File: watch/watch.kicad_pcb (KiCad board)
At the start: 2 copper layers, 36 x 36 mm, 102 parts, among them IC1 IS32FL3237-TQLA3-TR, SW1 ButtonWakeup, U1 STM32L031F4Px, Y1 CR_32kHz

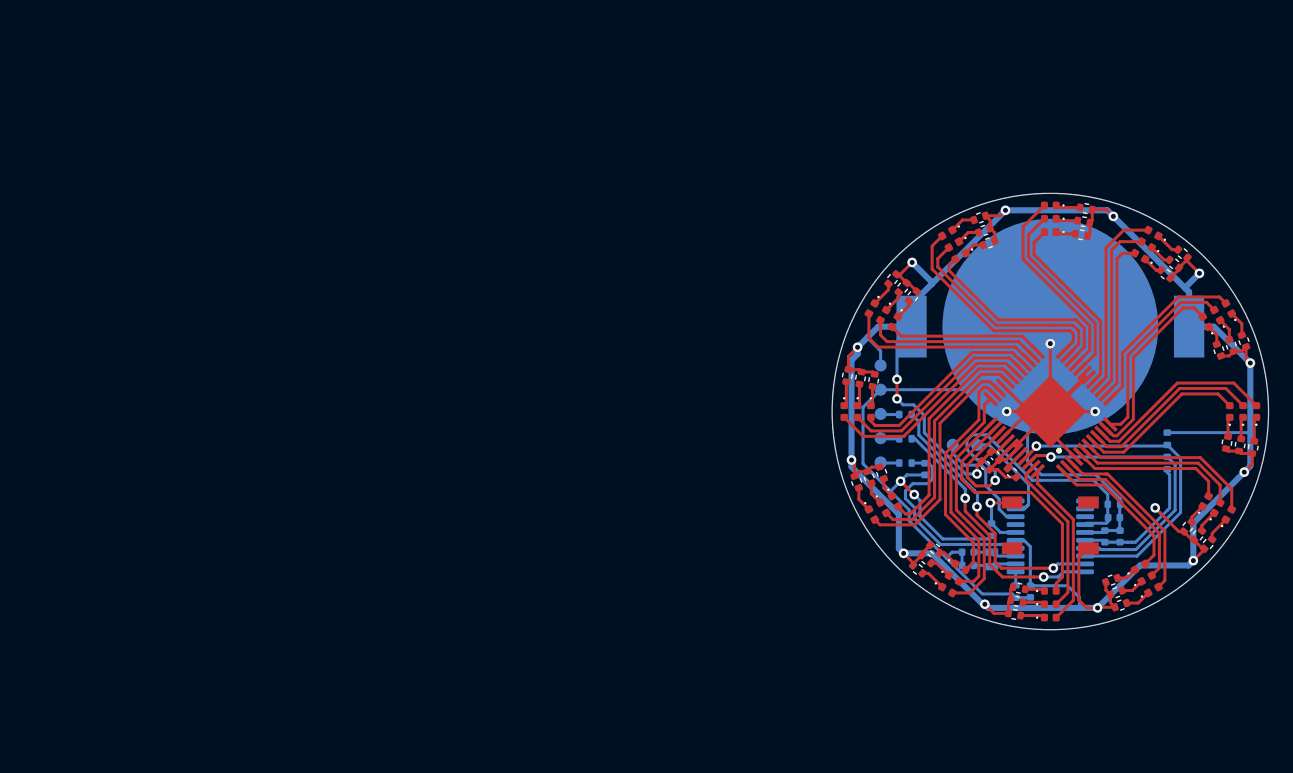
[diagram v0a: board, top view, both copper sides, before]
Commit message: 60 LED version
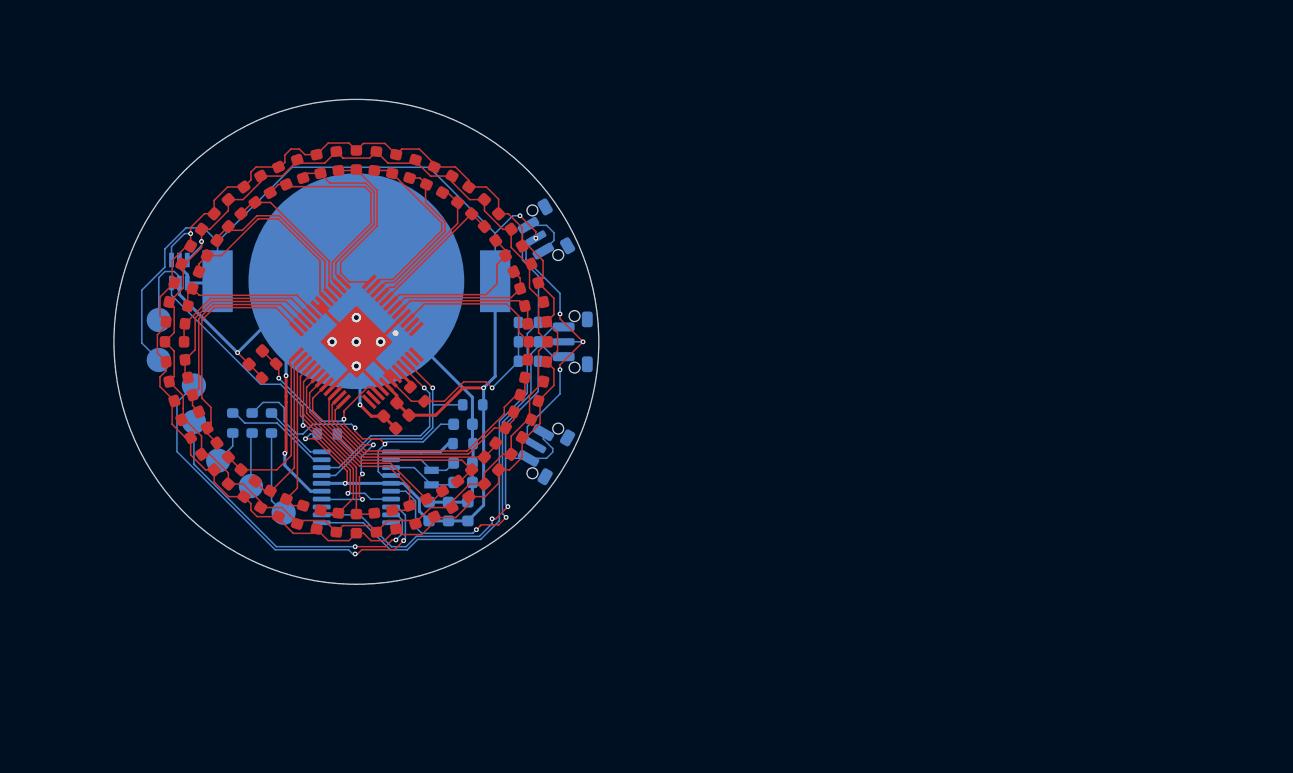
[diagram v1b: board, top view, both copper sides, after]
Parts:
- removed R10, R11, R12, R13, R14, R15, R16, R17, R18, R19, R21, R22, R23, R25, R26, R27, R29, R30, R32, R33, R34, R35, R36, R37, R38, R39, R40, R41, R42, R43, R44, R5, R6, R7, R8, R9: 660R, Resistor_SMD:R_0402_1005Metric
- added D37: LED_Small, custom:LED_0603_1608Metric, F.Cu at (108.8, 112.1)
- added D38: LED_Small, custom:LED_0603_1608Metric, F.Cu at (110.0, 111.1)
- added D39: LED_Small, custom:LED_0603_1608Metric, F.Cu at (111.1, 110.0)
- added D40: LED_Small, custom:LED_0603_1608Metric, F.Cu at (112.1, 108.8)
- added D41: LED_Small, custom:LED_0603_1608Metric, F.Cu at (113.0, 107.5)
- added D42: LED_Small, custom:LED_0603_1608Metric, F.Cu at (113.7, 106.1)
- added D43: LED_Small, custom:LED_0603_1608Metric, F.Cu at (114.3, 104.6)
- added D44: LED_Small, custom:LED_0603_1608Metric, F.Cu at (114.7, 103.1)
- added D45: LED_Small, custom:LED_0603_1608Metric, F.Cu at (114.9, 101.6)
- added D46: LED_Small, custom:LED_0603_1608Metric, F.Cu at (115.0, 100.0)
- added D47: LED_Small, custom:LED_0603_1608Metric, F.Cu at (114.9, 98.4)
- added D48: LED_Small, custom:LED_0603_1608Metric, F.Cu at (114.7, 96.9)
- added D49: LED_Small, custom:LED_0603_1608Metric, F.Cu at (114.3, 95.4)
- added D50: LED_Small, custom:LED_0603_1608Metric, F.Cu at (113.7, 93.9)
- added D51: LED_Small, custom:LED_0603_1608Metric, F.Cu at (113.0, 92.5)
- added D52: LED_Small, custom:LED_0603_1608Metric, F.Cu at (112.1, 91.2)
- added D53: LED_Small, custom:LED_0603_1608Metric, F.Cu at (111.1, 90.0)
- added D54: LED_Small, custom:LED_0603_1608Metric, F.Cu at (110.0, 88.9)
- added D55: LED_Small, custom:LED_0603_1608Metric, F.Cu at (108.8, 87.9)
- added D56: LED_Small, custom:LED_0603_1608Metric, F.Cu at (107.5, 87.0)
- added D57: LED_Small, custom:LED_0603_1608Metric, F.Cu at (106.1, 86.3)
- added D58: LED_Small, custom:LED_0603_1608Metric, F.Cu at (104.6, 85.7)
- added D59: LED_Small, custom:LED_0603_1608Metric, F.Cu at (103.1, 85.3)
- added D60: LED_Small, custom:LED_0603_1608Metric, F.Cu at (101.6, 85.1)
- added IC2: TMUX1237DCKR, SamacSys_Parts:SOT65P210X110-6N, B.Cu at (85.4, 94.2)
- added R45: 10k, custom:R_0603_1608Metric, B.Cu at (114.2, 98.4)
- added R46: 10k, custom:R_0603_1608Metric, B.Cu at (114.2, 101.6)
- added SW1: ButtonWakeup, Button_Switch_SMD:SW_Push_1P1T-MP_NO_Horizontal_Alps_SKRTLAE010, B.Cu at (118.0, 100.0)
- added SW2: ButtonUp, Button_Switch_SMD:SW_Push_1P1T-MP_NO_Horizontal_Alps_SKRTLAE010, B.Cu at (115.6, 91.0)
- BT1: footprint SamacSys_Parts:CR2032 -> BAT-HLD-001:BATHLD001
- C1, C3, C4, C5, C6, C7, C8, C9: footprint Capacitor_SMD:C_0402_1005Metric -> custom:C_0603_1608Metric
- C2: footprint Capacitor_SMD:C_0402_1005Metric -> custom:C_0603_1608Metric; moved to F.Cu
- D1, D10, D11, D12, D13, D14, D15, D16, D17, D18, D19, D2, D20, D21, D22, D23, D24, D25, D26, D27, D28, D29, D3, D30, D31, D32, D33, D34, D35, D36, D4, D5, D6, D7, D8, D9: value LED_ORNG -> LED_Small; footprint LED_SMD:LED_0402_1005Metric -> custom:LED_0603_1608Metric
- R1, R2, R28, R3, R31, R4, R51: footprint Resistor_SMD:R_0402_1005Metric -> custom:R_0603_1608Metric
- R20: footprint Resistor_SMD:R_0402_1005Metric -> custom:R_0603_1608Metric; moved to F.Cu
- R24: value 3.3k -> 3.8k; footprint Resistor_SMD:R_0402_1005Metric -> custom:R_0603_1608Metric
- SW3: renamed from SW1; value ButtonWakeup -> ButtonDown; footprint Button_Switch_SMD:SW_SPST_TL3342 -> Button_Switch_SMD:SW_Push_1P1T-MP_NO_Horizontal_Alps_SKRTLAE010; moved to B.Cu
- TP1, TP2, TP3, TP4, TP5, TP6, TP7: footprint TestPoint:TestPoint_Pad_D1.0mm -> TestPoint:TestPoint_Pad_D2.0mm
- moved D19 81.2 mm to (85.7, 104.6), turned to -162 degrees
- moved D20 80.2 mm to (86.3, 106.1), turned to -156 degrees
- moved D21 79.0 mm to (87.0, 107.5), turned to -150 degrees
- moved D22 77.4 mm to (87.9, 108.8), turned to -144 degrees
- moved D23 76.9 mm to (88.9, 110.0), turned to -138 degrees
- moved D12 76.6 mm to (86.3, 93.9), turned to 156 degrees
- moved D24 76.4 mm to (90.0, 111.1), turned to -132 degrees
- moved D11 76.0 mm to (87.0, 92.5), turned to 150 degrees
- moved D10 75.3 mm to (87.9, 91.2), turned to 144 degrees
- moved D28 74.7 mm to (95.4, 114.3), turned to -108 degrees
- moved D29 74.1 mm to (96.9, 114.7), turned to -102 degrees
- moved D30 73.5 mm to (98.4, 114.9), turned to -96 degrees
- moved D16 73.1 mm to (85.0, 100.0)
- moved D17 73.1 mm to (85.1, 101.6), turned to -174 degrees
- moved D18 72.9 mm to (85.3, 103.1), turned to -168 degrees
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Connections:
- D11 pad 2: Net-(D11-Pad2) -> Net-(D1-Pad2)
- D12 pad 1: Net-(D12-Pad1) -> Net-(D11-Pad1)
- D12 pad 2: Net-(D12-Pad2) -> Net-(D10-Pad2)
- D13 pad 2: Net-(D13-Pad2) -> Net-(D1-Pad2)
- D14 pad 1: Net-(D14-Pad1) -> Net-(D13-Pad1)
- D14 pad 2: Net-(D14-Pad2) -> Net-(D10-Pad2)
- D15 pad 2: Net-(D15-Pad2) -> Net-(D1-Pad2)
- D16 pad 1: Net-(D16-Pad1) -> Net-(D15-Pad1)
- D16 pad 2: Net-(D16-Pad2) -> Net-(D10-Pad2)
- D17 pad 2: Net-(D17-Pad2) -> Net-(D1-Pad2)
- D18 pad 1: Net-(D18-Pad1) -> Net-(D17-Pad1)
- D18 pad 2: Net-(D18-Pad2) -> Net-(D10-Pad2)
- D19 pad 2: Net-(D19-Pad2) -> Net-(D1-Pad2)
- D2 pad 1: Net-(D2-Pad1) -> Net-(D1-Pad1)
- D2 pad 2: Net-(D2-Pad2) -> Net-(D10-Pad2)
- D20 pad 1: Net-(D20-Pad1) -> Net-(D19-Pad1)
- D20 pad 2: Net-(D20-Pad2) -> Net-(D10-Pad2)
- D21 pad 2: Net-(D21-Pad2) -> Net-(D1-Pad2)
- D22 pad 1: Net-(D22-Pad1) -> Net-(D21-Pad1)
- D22 pad 2: Net-(D22-Pad2) -> Net-(D10-Pad2)
- D23 pad 2: Net-(D23-Pad2) -> Net-(D1-Pad2)
- D24 pad 1: Net-(D24-Pad1) -> Net-(D23-Pad1)
- D24 pad 2: Net-(D24-Pad2) -> Net-(D10-Pad2)
- D25 pad 2: Net-(D25-Pad2) -> Net-(D1-Pad2)
- D26 pad 1: Net-(D26-Pad1) -> Net-(D25-Pad1)
- D26 pad 2: Net-(D26-Pad2) -> Net-(D10-Pad2)
- D27 pad 2: Net-(D27-Pad2) -> Net-(D1-Pad2)
- D28 pad 1: Net-(D28-Pad1) -> Net-(D27-Pad1)
- D28 pad 2: Net-(D28-Pad2) -> Net-(D10-Pad2)
- D29 pad 2: Net-(D29-Pad2) -> Net-(D1-Pad2)
- D3 pad 2: Net-(D3-Pad2) -> Net-(D1-Pad2)
- D30 pad 1: Net-(D30-Pad1) -> Net-(D29-Pad1)
- D30 pad 2: Net-(D30-Pad2) -> Net-(D10-Pad2)
- D31 pad 2: Net-(D31-Pad2) -> Net-(D1-Pad2)
- D32 pad 1: Net-(D32-Pad1) -> Net-(D31-Pad1)
- D32 pad 2: Net-(D32-Pad2) -> Net-(D10-Pad2)
- D33 pad 2: Net-(D33-Pad2) -> Net-(D1-Pad2)
- D34 pad 1: Net-(D34-Pad1) -> Net-(D33-Pad1)
- D34 pad 2: Net-(D34-Pad2) -> Net-(D10-Pad2)
- D35 pad 2: Net-(D35-Pad2) -> Net-(D1-Pad2)
- D36 pad 1: Net-(D36-Pad1) -> Net-(D35-Pad1)
- D36 pad 2: Net-(D36-Pad2) -> Net-(D10-Pad2)
- D4 pad 1: Net-(D4-Pad1) -> Net-(D3-Pad1)
- D4 pad 2: Net-(D4-Pad2) -> Net-(D10-Pad2)
- D5 pad 2: Net-(D5-Pad2) -> Net-(D1-Pad2)
- D6 pad 1: Net-(D6-Pad1) -> Net-(D5-Pad1)
- D6 pad 2: Net-(D6-Pad2) -> Net-(D10-Pad2)
- D7 pad 2: Net-(D7-Pad2) -> Net-(D1-Pad2)
- D8 pad 1: Net-(D8-Pad1) -> Net-(D7-Pad1)
- D8 pad 2: Net-(D8-Pad2) -> Net-(D10-Pad2)
- D9 pad 1: Net-(D9-Pad1) -> Net-(D10-Pad1)
- D9 pad 2: Net-(D9-Pad2) -> Net-(D1-Pad2)
- IC1 pad 1: Net-(D22-Pad2) -> unconnected-(IC1-Pad1)
- IC1 pad 10: Net-(D33-Pad2) -> Net-(D57-Pad1)
- IC1 pad 11: Net-(D34-Pad2) -> Net-(D59-Pad1)
- IC1 pad 12: Net-(D35-Pad2) -> Net-(D1-Pad1)
- IC1 pad 13: Net-(D36-Pad2) -> Net-(D3-Pad1)
- IC1 pad 14: Net-(D21-Pad2) -> Net-(D5-Pad1)
- IC1 pad 15: Net-(D20-Pad2) -> Net-(D7-Pad1)
- IC1 pad 16: Net-(D19-Pad2) -> Net-(D10-Pad1)
- IC1 pad 17: Net-(D18-Pad2) -> Net-(D11-Pad1)
- IC1 pad 2: Net-(D23-Pad2) -> unconnected-(IC1-Pad2)
- IC1 pad 20: Net-(D17-Pad2) -> Net-(D13-Pad1)
- IC1 pad 21: Net-(D16-Pad2) -> Net-(D15-Pad1)
- IC1 pad 22: Net-(D27-Pad2) -> Net-(D17-Pad1)
- IC1 pad 23: Net-(D26-Pad2) -> Net-(D19-Pad1)
- IC1 pad 24: Net-(D25-Pad2) -> Net-(D21-Pad1)
- IC1 pad 25: Net-(D15-Pad2) -> Net-(D23-Pad1)
- IC1 pad 26: Net-(D14-Pad2) -> Net-(D25-Pad1)
- IC1 pad 27: Net-(D13-Pad2) -> Net-(D27-Pad1)
- IC1 pad 28: Net-(D1-Pad2) -> Net-(D29-Pad1)
- IC1 pad 29: Net-(D2-Pad2) -> Net-(D31-Pad1)
- IC1 pad 3: Net-(D24-Pad2) -> Net-(D45-Pad1)
- IC1 pad 30: Net-(D3-Pad2) -> Net-(D33-Pad1)
- IC1 pad 31: Net-(D4-Pad2) -> Net-(D35-Pad1)
- IC1 pad 32: Net-(D5-Pad2) -> Net-(D37-Pad1)
- IC1 pad 34: Net-(D6-Pad2) -> Net-(D39-Pad1)
- IC1 pad 35: Net-(D7-Pad2) -> Net-(D41-Pad1)
- IC1 pad 36: Net-(D8-Pad2) -> Net-(D43-Pad1)
- IC1 pad 37: Net-(D9-Pad2) -> unconnected-(IC1-Pad37)
- IC1 pad 38: Net-(D10-Pad2) -> unconnected-(IC1-Pad38)
- IC1 pad 47: Net-(D11-Pad2) -> unconnected-(IC1-Pad47)
- IC1 pad 48: Net-(D12-Pad2) -> unconnected-(IC1-Pad48)
- IC1 pad 5: Net-(D28-Pad2) -> Net-(D47-Pad1)
- IC1 pad 6: Net-(D29-Pad2) -> Net-(D49-Pad1)
- IC1 pad 7: Net-(D30-Pad2) -> Net-(D51-Pad1)
- IC1 pad 8: Net-(D31-Pad2) -> Net-(D53-Pad1)
- IC1 pad 9: Net-(D32-Pad2) -> Net-(D55-Pad1)
- SW3 pad 1: Net-(R51-Pad1) -> Net-(R46-Pad1)
- U1 pad 10: Net-(U1-Pad10) -> unconnected-(U1-Pad10)
- U1 pad 12: Net-(U1-Pad12) -> Net-(R46-Pad1)
- U1 pad 13: Net-(U1-Pad13) -> unconnected-(U1-Pad13)
- U1 pad 7: Net-(U1-Pad7) -> /LED_Driver/LED_BANK
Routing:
- net +3V3: track 258.7 -> 138.0 mm, vias 16 -> 8
- net Net-(D1-Pad2): track 16.0 -> 122.6 mm, vias 0 -> 1
- net Net-(D10-Pad2): track 20.9 -> 113.7 mm, vias 0 -> 1
- net Net-(R45-Pad1): track 0.00 -> 48.1 mm
- net Net-(R46-Pad1): track 0.00 -> 38.1 mm, vias 0 -> 2
- net /LED_Driver/LED_BANK: track 0.00 -> 28.5 mm, vias 0 -> 2
- net Net-(R51-Pad1): track 6.11 -> 34.3 mm, vias 1 -> 2
- net Net-(TP6-Pad1): track 9.32 -> 32.4 mm, vias 0 -> 2
- net Net-(D43-Pad1): track 0.00 -> 21.9 mm
- net Net-(D41-Pad1): track 0.00 -> 20.1 mm
- net Net-(D37-Pad1): track 0.00 -> 19.3 mm
- net Net-(D6-Pad2): track 19.3 -> 0.00 mm
- net Net-(D5-Pad2): track 19.1 -> 0.00 mm
- net Net-(D21-Pad1): track 1.68 -> 20.6 mm
- net Net-(D8-Pad2): track 18.8 -> 0.00 mm
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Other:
- board size 36 x 36 mm -> 40 x 40 mm
- net class Default removed
- board text added: "3V3"
- board text added: "GND"
- board text added: "RX"
- board text added: "SWCLK"
- board text added: "SWIO"
- board text added: "SWRST"
- board text added: "TX"
- board text added: "V1.2"
- board text removed: "V1.0"

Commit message: as ordered
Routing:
- net GND: track 135.5 -> 129.5 mm
- net +3V3: track 138.0 -> 135.5 mm
- net Net-(R51-Pad1): track 34.3 -> 32.6 mm, vias 2 -> 0
- net Net-(R45-Pad1): track 48.1 -> 47.2 mm, vias 0 -> 2
- net Net-(R46-Pad1): track 38.1 -> 37.7 mm, vias 2 -> 0
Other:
- outline, holes or cut-outs redrawn
- board text added: "1"
- board text added: "10"
- board text added: "11"
- board text added: "12"
- board text added: "2"
- board text added: "3"
- board text added: "4"
- board text added: "5"
- board text added: "6"
- board text added: "7"
- board text added: "8"
- board text added: "9"

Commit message: as ordered V1.4
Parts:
- removed R28, R31: 2k, custom:R_0603_1608Metric
- removed TP6: UART_TX, TestPoint:TestPoint_Pad_D2.0mm
- removed TP7: UART_RX, TestPoint:TestPoint_Pad_D2.0mm
- added C10: 10uF, custom:C_0603_1608Metric, B.Cu at (86.8, 96.6)
- added L1: 4.7uH, Inductor_SMD:L_0603_1608Metric_Pad1.05x0.95mm_HandSolder, B.Cu at (89.2, 99.9)
- added Q1: RU1C002UNTCL, mrab:SOT-323FL, B.Cu at (89.7, 104.2)
- added R5: 2k, custom:R_0603_1608Metric, B.Cu at (97.7, 105.8)
- added R6: 2k, custom:R_0603_1608Metric, B.Cu at (94.6, 105.8)
- added R7: 10k, custom:R_0603_1608Metric, B.Cu at (90.4, 109.2)
- added R8: 2k, custom:R_0603_1608Metric, B.Cu at (93.2, 103.5)
- added VR1: XC9140331MR-G, mrab:SOT-25, B.Cu at (86.8, 99.9)
- BT1: footprint BAT-HLD-001:BATHLD001 -> SamacSys_Parts:BATHLD001
- C2: value 100nF -> 4.7uF; moved to B.Cu
- TP1: value SWD_3V3 -> SWD_BAT
- moved TP1 29.5 mm to (111.3, 111.9)
- moved TP2 29.5 mm to (111.3, 108.6)
- moved C5 18.8 mm to (90.4, 114.0), turned to 0 degrees
- moved C7 17.5 mm to (90.4, 110.8), turned to 0 degrees
- moved TP5 17.2 mm to (108.4, 113.8), turned to 20 degrees
- moved C6 15.7 mm to (90.4, 112.4), turned to 0 degrees
- moved TP3 15.2 mm to (102.4, 116.0), turned to 20 degrees
- moved IC2 14.0 mm to (87.0, 108.1)
- moved R3 12.2 mm to (99.6, 115.8)
- moved R1 12.2 mm to (97.0, 116.6), turned to 0 degrees
- moved TP4 11.4 mm to (105.4, 114.9), turned to 20 degrees
- moved R20 10.7 mm to (102.1, 107.7), turned to -45 degrees
- moved R2 9.21 mm to (97.0, 115.0), turned to 0 degrees
- moved C2 7.43 mm to (84.4, 99.9), turned to 90 degrees
- moved C1 6.63 mm to (103.3, 110.5)
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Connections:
- BT1 pad 1: +3V3 -> +BATT
- C2 pad 1: /LED_Driver/EN -> +BATT
- C2 pad 2: GND -> GND1
- C3 pad 1: GND -> GND1
- C3 pad 2: +3V3 -> /LED_Driver/VCC_LED
- C4 pad 1: GND -> GND1
- C4 pad 2: +3V3 -> /LED_Driver/VCC_LED
- C5 pad 2: +3V3 -> +BATT
- C6 pad 2: +3V3 -> +BATT
- C7 pad 2: +3V3 -> +BATT
- IC1 pad 18: GND -> GND1
- IC1 pad 19: GND -> GND1
- IC1 pad 33: GND -> GND1
- IC1 pad 39: /LED_Driver/EN -> Net-(IC1-Pad39)
- IC1 pad 4: GND -> GND1
- IC1 pad 40: GND -> GND1
- IC1 pad 41: +3V3 -> /LED_Driver/VCC_LED
- IC1 pad 42: GND -> GND1
- IC1 pad 43: GND -> GND1
- IC1 pad 49: GND -> GND1
- IC2 pad 2: +3V3 -> /LED_Driver/VCC_LED
- IC2 pad 4: +3V3 -> /LED_Driver/VCC_LED
- IC2 pad 5: GND -> GND1
- IC2 pad 6: /LED_Driver/LED_BANK -> Net-(IC2-Pad6)
- R20 pad 1: /LED_Driver/EN -> Net-(IC1-Pad39)
- R20 pad 2: GND -> /LED_Driver/VCC_LED
- R24 pad 1: GND -> GND1
- SW1 pad 2: +3V3 -> +BATT
- SW2 pad 2: +3V3 -> +BATT
- SW3 pad 2: +3V3 -> +BATT
- TP1 pad 1: +3V3 -> +BATT
- U1 pad 10: unconnected-(U1-Pad10) -> /LED_Driver/LED_BANK
- U1 pad 11: Net-(R45-Pad1) -> unconnected-(U1-Pad11)
- U1 pad 12: Net-(R46-Pad1) -> unconnected-(U1-Pad12)
- U1 pad 14: /LED_Driver/EN -> unconnected-(U1-Pad14)
- U1 pad 16: +3V3 -> +BATT
- U1 pad 5: +3V3 -> +BATT
- U1 pad 7: /LED_Driver/LED_BANK -> Net-(R45-Pad1)
- U1 pad 8: Net-(TP6-Pad1) -> Net-(R46-Pad1)
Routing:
- net +BATT: track 0.00 -> 161.0 mm, vias 0 -> 11
- net +3V3: track 135.5 -> 0.00 mm, vias 8 -> 0
- net GND1: track 0.00 -> 81.6 mm, vias 0 -> 3
- net GND: track 129.5 -> 75.5 mm, vias 10 -> 12
- net /LED_Driver/VCC_LED: track 0.00 -> 46.9 mm, vias 0 -> 4
- net Net-(TP6-Pad1): track 32.3 -> 0.00 mm, vias 2 -> 0
- net /LED_Driver/EN: track 26.4 -> 0.00 mm, vias 5 -> 0
- net /LED_Driver/LED_BANK: track 28.4 -> 12.4 mm
- net Net-(R45-Pad1): track 47.2 -> 32.6 mm
- net Net-(U1-Pad9): track 26.2 -> 12.0 mm
- net nRST: track 24.3 -> 14.7 mm
- net Net-(R46-Pad1): track 37.7 -> 29.9 mm
- net Net-(D21-Pad1): track 20.6 -> 12.9 mm
- net Net-(R3-Pad2): track 4.42 -> 10.6 mm
- net Net-(D5-Pad1): track 18.2 -> 12.0 mm
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- added copper zone on B.Cu, net GND
- added copper zone on F.Cu, net GND
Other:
- board size 40 x 40 mm -> 38 x 38 mm
- board text added: "SWDCLK"
- board text added: "SWDIO"
- board text added: "SWDRST"
- board text added: "V1.4"
- board text removed: "1"
- board text removed: "10"
- board text removed: "11"
- board text removed: "12"
- board text removed: "2"
- board text removed: "3"
- board text removed: "4"
- board text removed: "5"
- board text removed: "6"
- board text removed: "7"
- board text removed: "8"
- board text removed: "9"
- board text removed: "RX"
- board text removed: "SWCLK"
- board text removed: "SWIO"
- board text removed: "SWRST"
- board text removed: "TX"
- board text removed: "V1.2"
